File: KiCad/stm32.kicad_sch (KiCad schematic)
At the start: 16 parts, among them J15 JACK-USBE-20PINTL, Q4 Q_Dual_PMOS_S1G1S2G2D2D2D1D1, Q5 2n7000, Q6 Q_Dual_PMOS_S1G1S2G2D2D2D1D1, Q7 2n7000, U3 STM32G071CBU6, Y6 25MHz

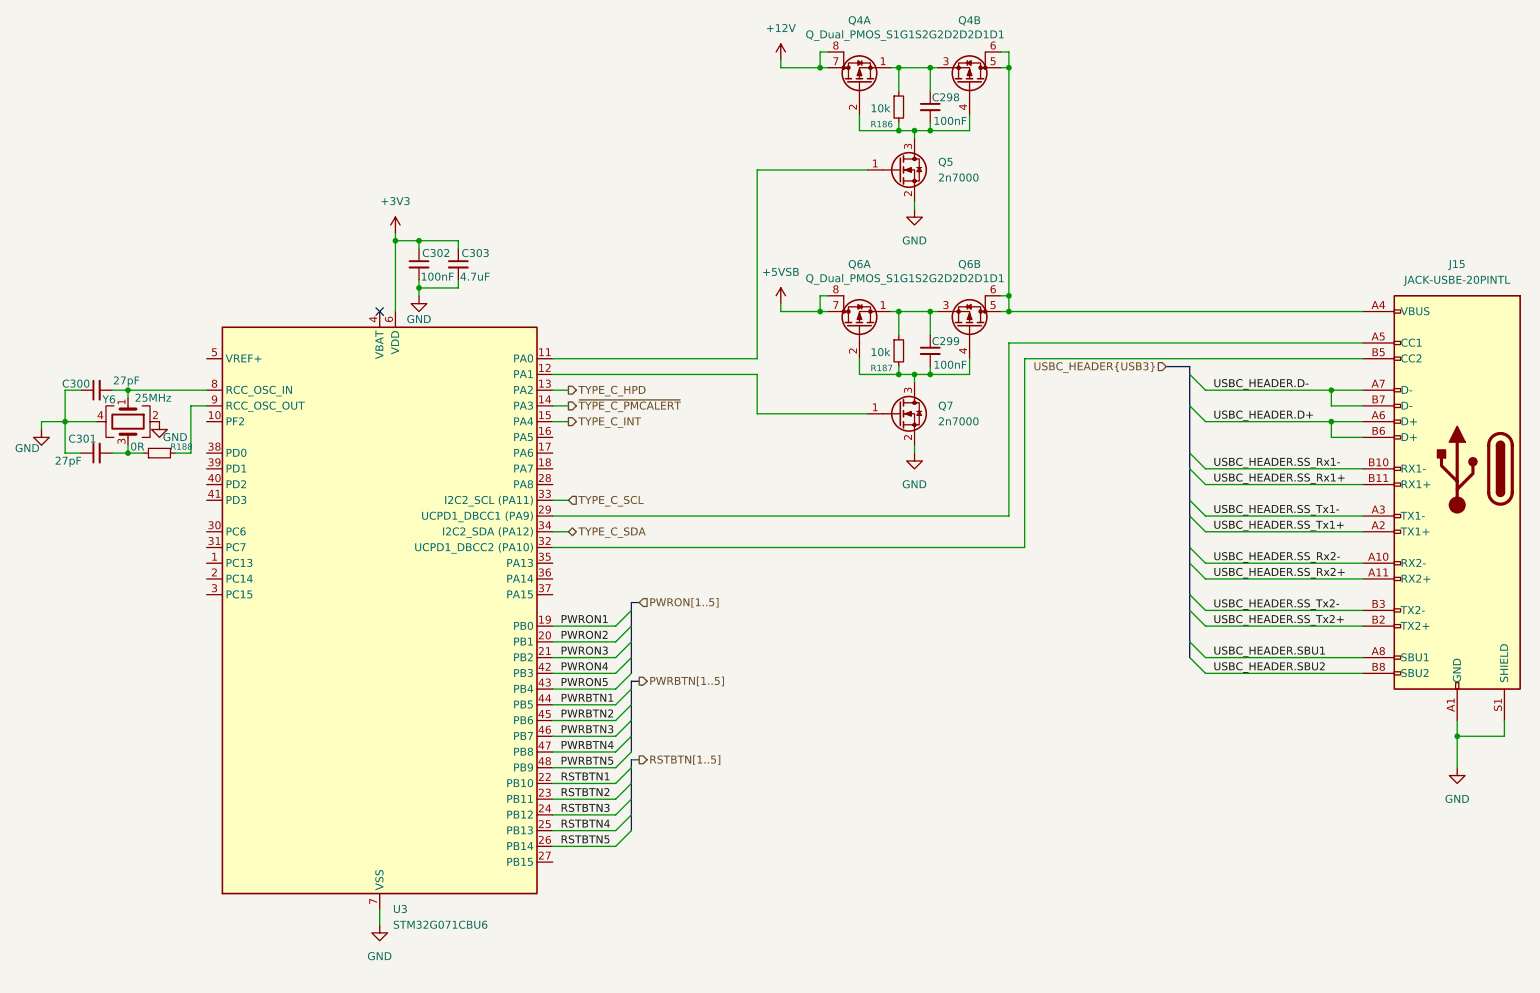
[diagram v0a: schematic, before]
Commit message: Add programming header and power and reset switches
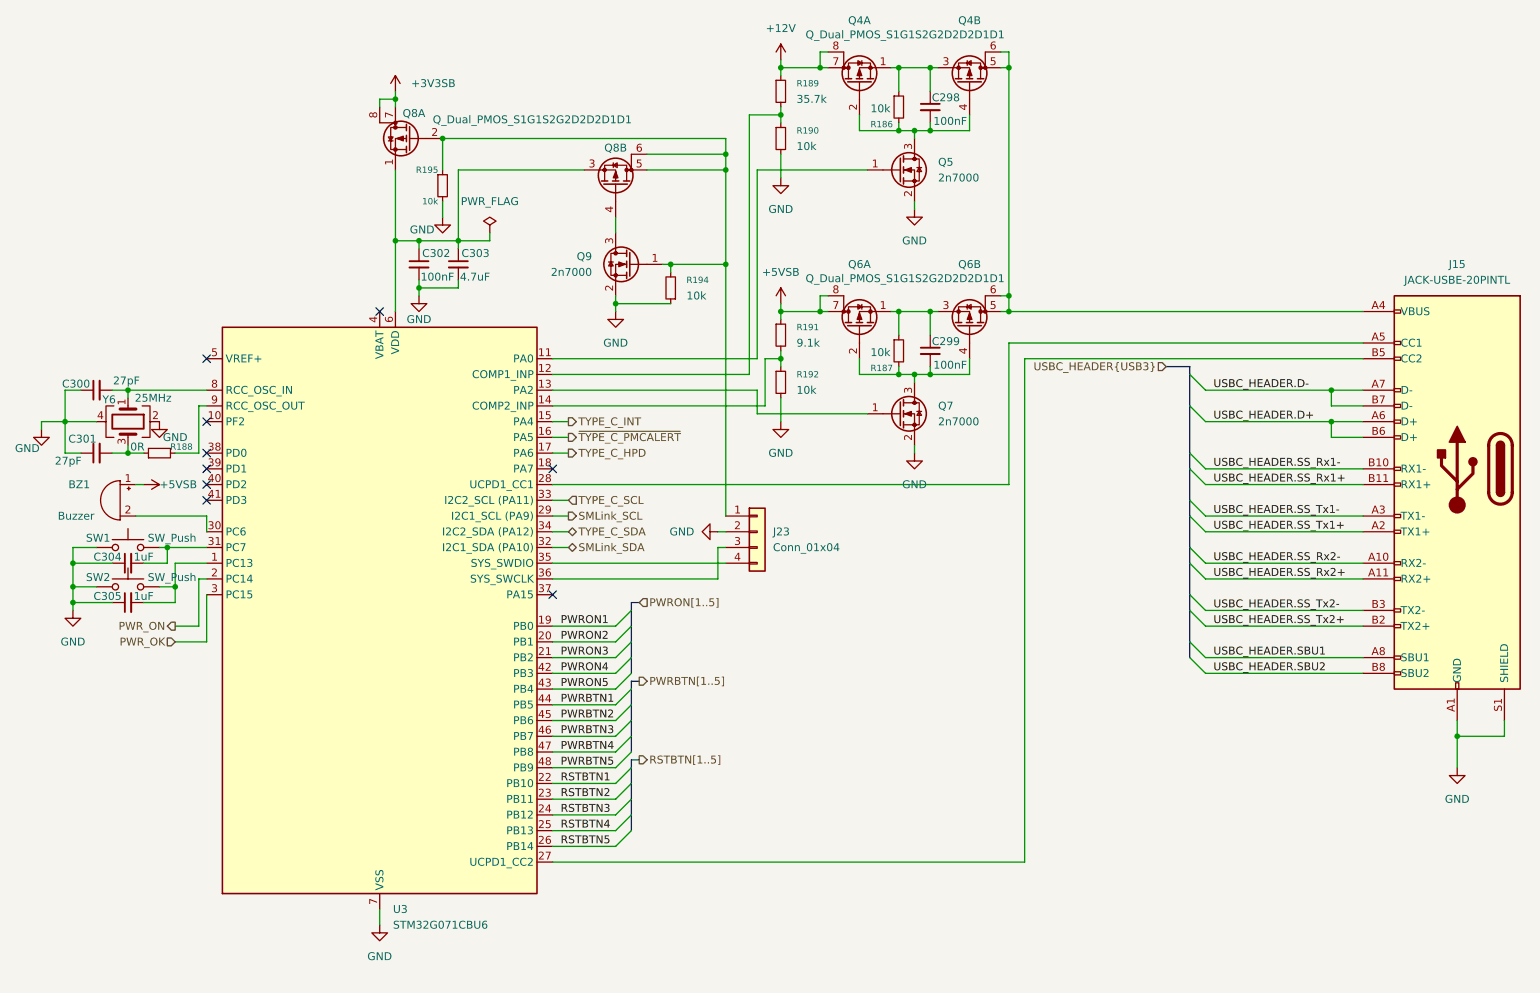
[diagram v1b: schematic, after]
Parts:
- added BZ1: Buzzer, symbol Device:Buzzer
- added C304, C305: 1uF, symbol Device:C_Small
- added J23: Conn_01x04, symbol Connector_Generic:Conn_01x04
- added Q8: Q_Dual_PMOS_S1G1S2G2D2D2D1D1, symbol Transistor_FET:Q_Dual_PMOS_S1G1S2G2D2D2D1D1
- added Q9: 2n7000, symbol Transistor_FET:Q_NMOS_GSD
- added R189: 35.7k, symbol Device:R_Small
- added R190, R192, R194, R195: 10k, symbol Device:R_Small
- added R191: 9.1k, symbol Device:R_Small
- added SW1, SW2: SW_Push, symbol Switch:SW_Push
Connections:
- net +12V: now also R189.1
- net +5VSB: now also BZ1.1 (+), R191.1
- net GND: now also C304.1, C305.1, J23.2 (Pin_2), Q9.2 (S), R190.2, R192.2, R194.1, R195.2, SW1.1, SW2.1
- net TYPE_C_HPD: now also U3.17 (PA6); no longer U3.13 (PA2)
- net ~{TYPE_C_PMCALERT}: now also U3.16 (PA5); no longer U3.14 (PA3)
- net at J15.A5 (CC1): now also U3.28 (PA8); no longer U3.29 (PA9/UCPD1_DBCC1)
- net at J15.B5 (CC2): now also U3.27 (PB15); no longer U3.32 (PA10/UCPD1_DBCC2)
- net at U3.12 (PA1): now also R189.2, R190.1; no longer Q7.1 (G)
- net at U3.1 (PC13): now also C305.2, SW2.2
- net PWR_ON: now reaches U3.2 (PC14)
- net PWR_OK: now reaches U3.3 (PC15)
- net at U3.30 (PC6): now also BZ1.2 (-)
- net at U3.31 (PC7): now also C304.2, SW1.2
- net at U3.35 (PA13): now also J23.4 (Pin_4)
- net at U3.36 (PA14): now also J23.3 (Pin_3)
- net +3V3: no longer names the net of C302.1, C303.1, U3.6 (VDD)
- net +3V3: now also Q8.1 (S), Q8.3 (S)
- new net: J23.1 (Pin_1), Q8.2 (G), Q8.5 (D), Q8.6 (D), Q9.1 (G), R194.2, R195.1
- new net: Q7.1 (G), U3.13 (PA2)
- new net: R191.2, R192.1, U3.14 (PA3)
- new net: Q8.4 (G), Q9.3 (D)
- new net +3V3SB: Q8.7 (D), Q8.8 (D)
- new net SMLink_SCL: U3.29 (PA9/UCPD1_DBCC1)
- new net SMLink_SDA: U3.32 (PA10/UCPD1_DBCC2)
- no-connect marks 1 -> 9

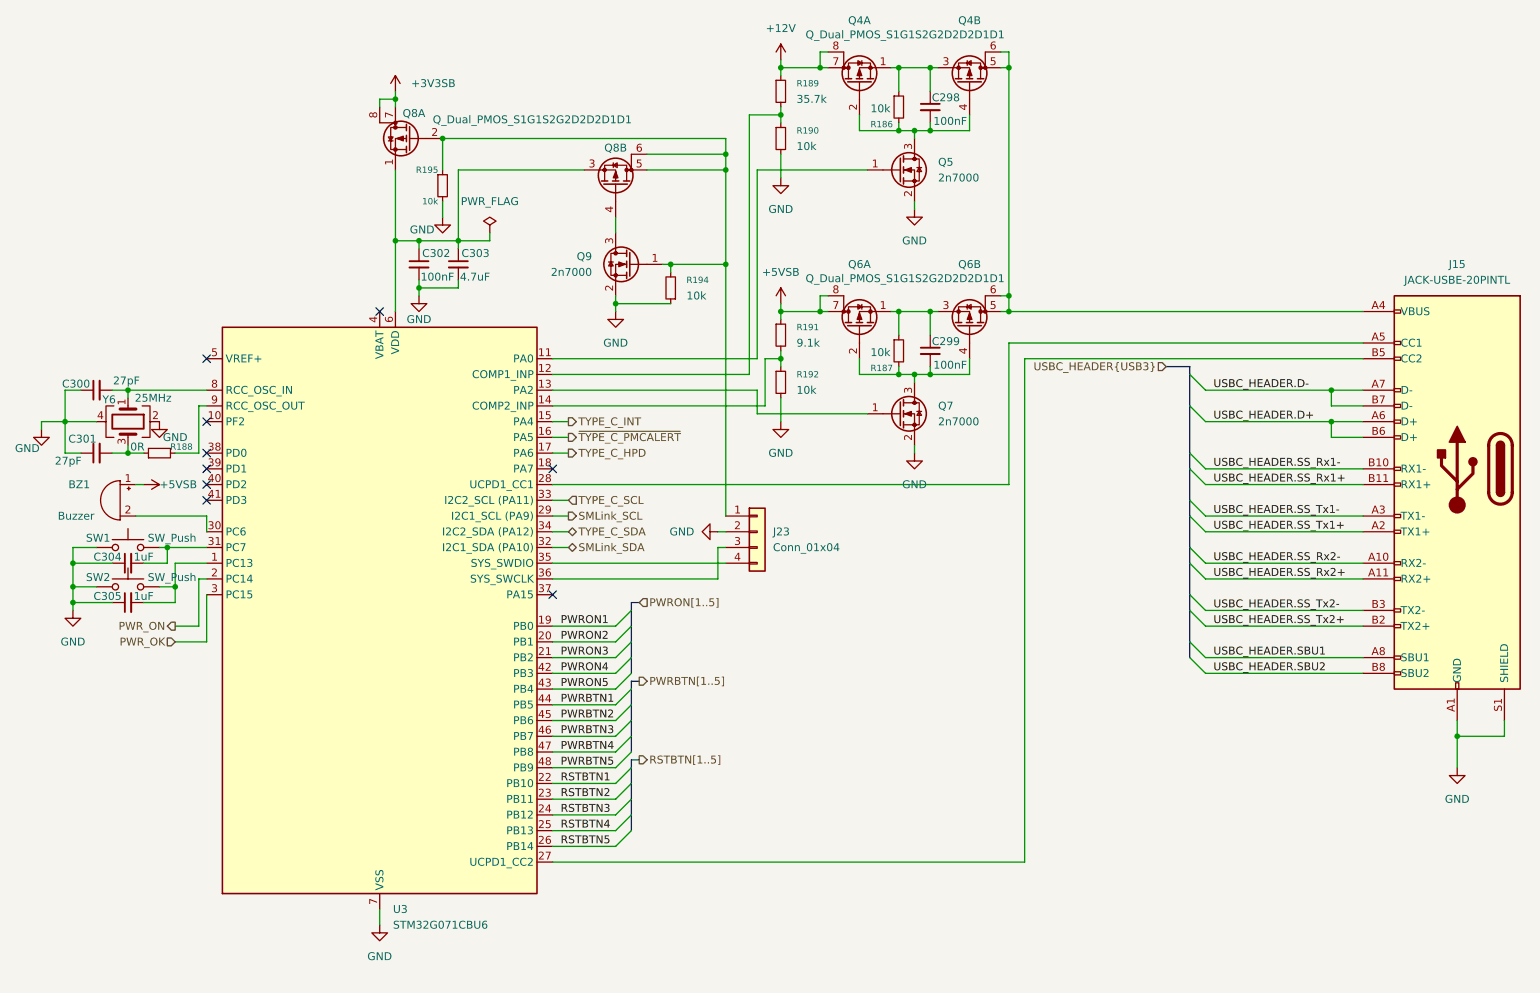
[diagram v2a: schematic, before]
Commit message: Add TPS65987D PD controller, switch stm32 to cheaper one
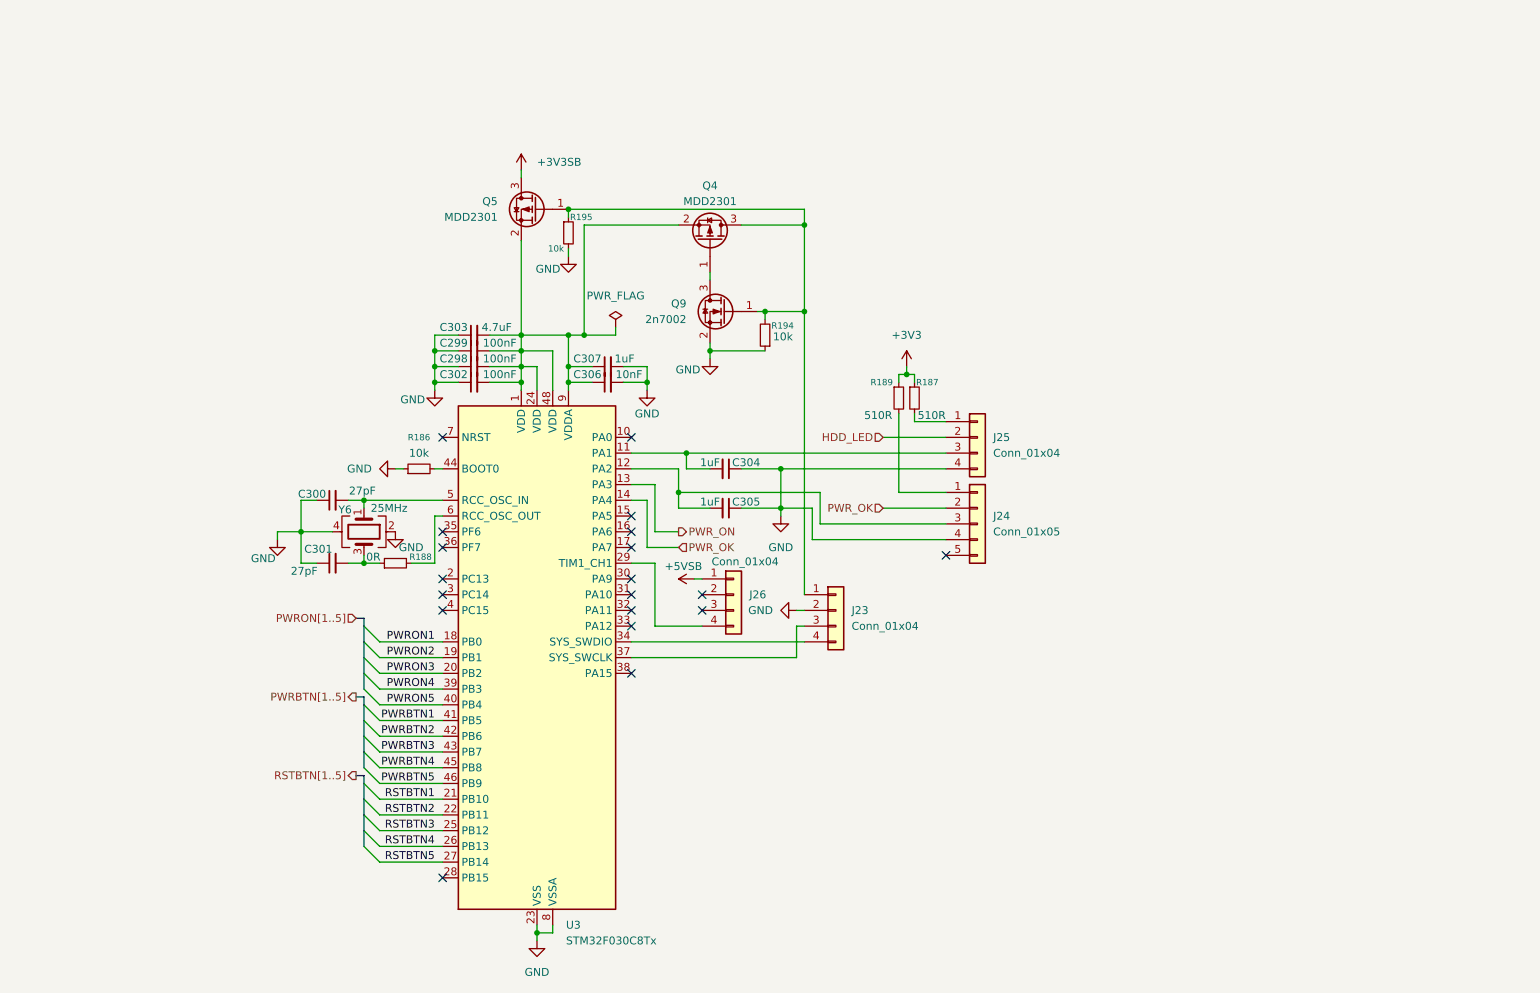
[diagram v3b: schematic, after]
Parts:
- removed BZ1: Buzzer, symbol Device:Buzzer
- removed J15: JACK-USBE-20PINTL, symbol Connector:USB_C_Receptacle
- removed Q4, Q6, Q8: Q_Dual_PMOS_S1G1S2G2D2D2D1D1, symbol Transistor_FET:Q_Dual_PMOS_S1G1S2G2D2D2D1D1
- removed Q5, Q7: 2n7000, symbol Transistor_FET:Q_NMOS_GSD
- removed R190, R192: 10k, symbol Device:R_Small
- removed R191: 9.1k, symbol Device:R_Small
- removed SW1, SW2: SW_Push, symbol Switch:SW_Push
- removed U3: STM32G071CBU6, Package_DFN_QFN:QFN-48-1EP_7x7mm_P0.5mm_EP5.6x5.6mm, symbol MCU_ST_STM32G0:STM32G0B1CBUx
- added C306: 10nF, symbol Device:C_Small
- added C307: 1uF, symbol Device:C_Small
- added J24: Conn_01x05, symbol Connector_Generic:Conn_01x05
- added J25, J26: Conn_01x04, symbol Connector_Generic:Conn_01x04
- added Q4, Q5: MDD2301, symbol Transistor_FET:Q_PMOS_GSD
- added U3: STM32F030C8Tx, Package_QFP:LQFP-48_7x7mm_P0.5mm, symbol MCU_ST_STM32F0:STM32F030C8Tx
- Q9: value 2n7000 -> 2n7002
- R187: value 10k -> 510R
- R189: value 35.7k -> 510R
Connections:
- net +12V is gone; now on net +3V3: R189.1
- net +3V3SB: now also Q5.3 (D)
- net +5VSB: now also J26.1 (Pin_1)
- net GND: now also C298.1, C299.1, C302.1, C303.1, R186.1, C306.2, C307.2, J24.4 (Pin_4), J25.4 (Pin_4), U3.23 (VSS), U3.47 (VSS), U3.8 (VSSA); no longer C302.2, C303.2
- net PWRBTN1: now also U3.41 (PB5)
- net PWRBTN2: now also U3.42 (PB6)
- net PWRBTN3: now also U3.43 (PB7)
- net PWRBTN4: now also U3.45 (PB8)
- net PWRBTN5: now also U3.46 (PB9)
- net PWRON1: now also U3.18 (PB0)
- net PWRON2: now also U3.19 (PB1)
- net PWRON3: now also U3.20 (PB2)
- net PWRON4: now also U3.39 (PB3)
- net PWRON5: now also U3.40 (PB4)
- net PWR_OK: now also J24.2 (Pin_2), U3.14 (PA4)
- net PWR_ON: now also U3.13 (PA3)
- net RSTBTN1: now also U3.21 (PB10)
- net RSTBTN2: now also U3.22 (PB11)
- net RSTBTN3: now also U3.25 (PB12)
- net RSTBTN4: now also U3.26 (PB13)
- net RSTBTN5: now also U3.27 (PB14)
- net at J23.1 (Pin_1), Q9.1 (G), R194.2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: now also Q4.3 (D), Q5.1 (G)
- net at R189.2: now also J24.1 (Pin_1)
- net at J23.3 (Pin_3): now also U3.37 (PA14)
- net at J23.4 (Pin_4): now also U3.34 (PA13)
- net at C298.2: now also C299.2, C302.2, C303.2, C306.1, C307.1, Q4.2 (S), Q5.2 (S), U3.1 (VDD), U3.24 (VDD), U3.48 (VDD), U3.9 (VDDA); no longer R186.2
- net at R187.2: now also J25.1 (Pin_1); no longer C299.2
- net +3V3: now reaches R187.1
- net +3V3: no longer C299.1
- net at Q9.3 (D): now also Q4.1 (G)
- net at C304.2: now also J25.3 (Pin_3), U3.11 (PA1)
- net at C305.2: now also J24.3 (Pin_3), U3.12 (PA2)
- net at C300.2, Y6.1: now also U3.5 (PF0)
- net at R188.2: now also U3.6 (PF1)
- new net: R186.2, U3.44 (BOOT0)
- new net: J26.4 (Pin_4), U3.29 (PA8)
- new net HDD_LED: J25.2 (Pin_2)
- no-connect marks 9 -> 19
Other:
- moved on the sheet: C300, C301, C302, C303, C304, C305, J23, Q9, R188, R194, R195, Y6

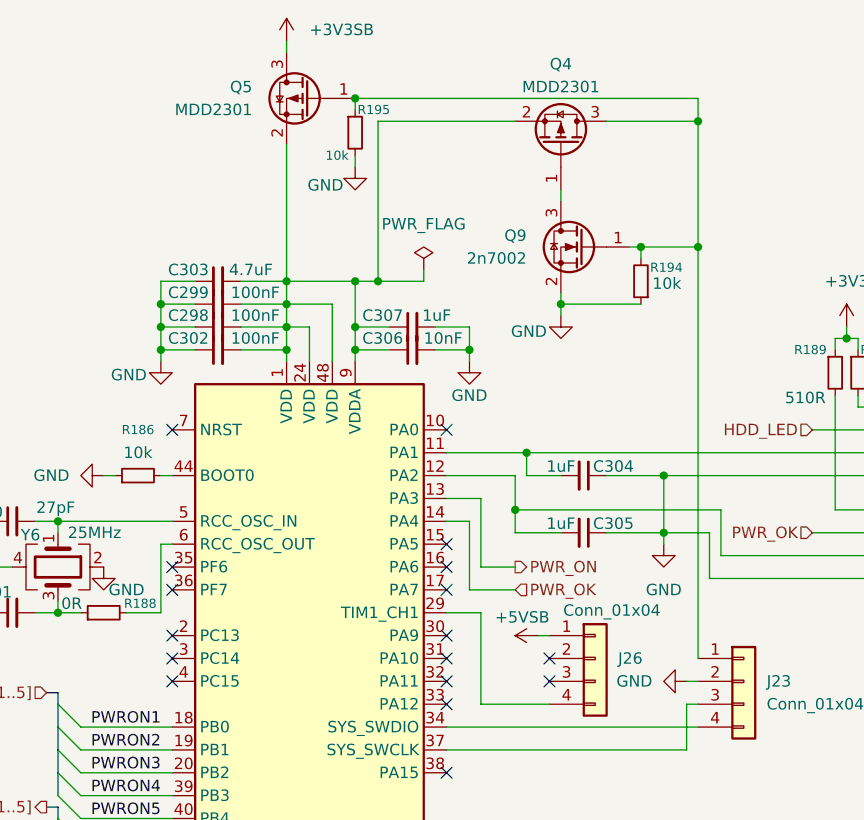
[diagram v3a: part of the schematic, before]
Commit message: Fix some diodes and resistors
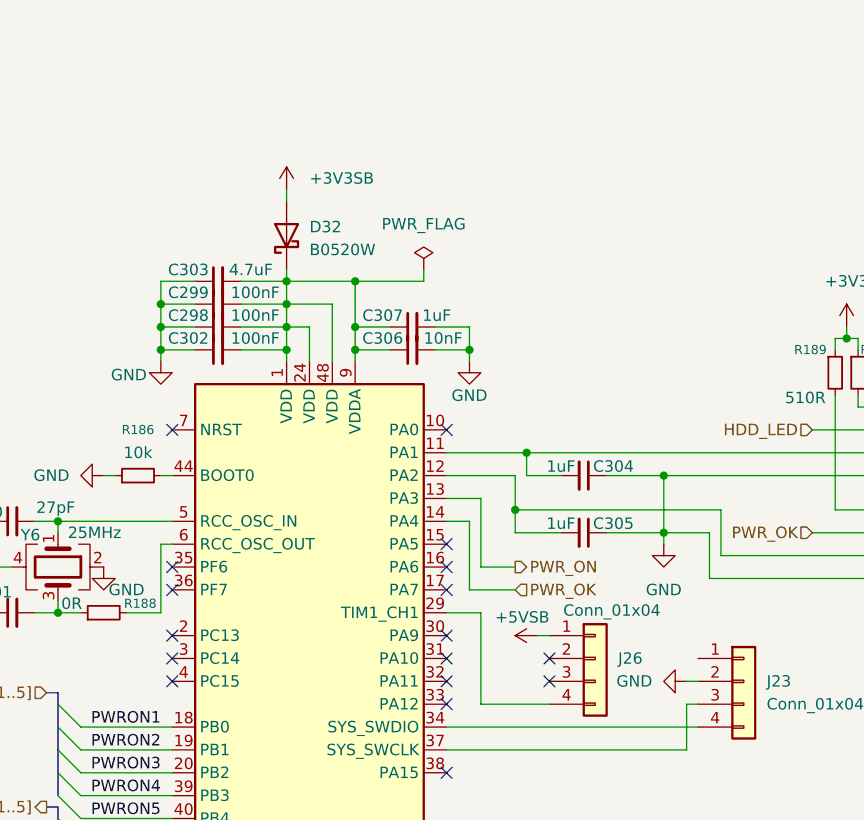
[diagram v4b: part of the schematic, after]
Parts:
- removed Q4, Q5: MDD2301, symbol Transistor_FET:Q_PMOS_GSD
- removed Q9: 2n7002, symbol Transistor_FET:Q_NMOS_GSD
- removed R194, R195: 10k, symbol Device:R_Small
- added D32: B0520W, Diode_SMD:D_SOD-123, symbol Device:D_Schottky
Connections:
- net +3V3SB: now also D32.2 (A)
- net at C298.2, C299.2, C302.2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: now also D32.1 (K)

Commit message: Work though ERC errors
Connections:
- net at C298.2, C299.2, C302.2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: now also J23.1 (Pin_1)
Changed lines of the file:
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@@
+	)
+	(junction
+		(at 133.35 72.39)
+		(diameter 0)
+		(color 0 0 0 0)
 	)
 	(junction
@@
 	(wire
 		(pts
+			(xy 163.83 72.39) (xy 133.35 72.39)
+		)
+		(stroke
+			(width 0)
+			(type default)
+		)
+	)
+	(wire
+		(pts
 			(xy 118.11 72.39) (xy 118.11 74.93)
 		)
@@
 		)
 		(stroke
+			(width 0)
+			(type default)
+		)
+	)
+	(wire
+		(pts
+			(xy 163.83 114.3) (xy 163.83 72.39)
+		)
+		(stroke

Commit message: Re-annotate components
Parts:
- renumbered C300 to C183, C301 to C184, C303 to C185, C299 to C186, C298 to C187, C302 to C188, C307 to C189, C306 to C190, C304 to C191, C305 to C192, D32 to D27, J26 to J15, J23 to J16, J25 to J17, J24 to J18, R188 to R113, R186 to R114, R189 to R115, R187 to R116, U3 to U7, Y6 to Y1
